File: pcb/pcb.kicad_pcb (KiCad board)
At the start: 2 copper layers, 350 x 170 mm, 80 parts, among them J1 Conn_01x24, SW1 0, SW10 9, SW11 HYPHEN, SW12 CARET, SW13 YEN, SW14 AT, SW15 LBRACKET, SW16 SEMICOLON, SW17 COLON, SW18 RBRACKET, SW19 COMMA, SW2 1, SW20 FULLSTOP, SW21 SLASH, SW22 UNDERSCORE, SW23 A, SW24 B, SW25 C, SW26 D, SW27 E, SW28 F, SW29 G, SW3 2, SW30 H, SW31 I, SW32 J, SW33 K, SW34 L, SW35 M, SW36 N, SW37 O, SW38 P, SW39 Q, SW4 3, SW40 R, SW41 PAUSE, SW42 S, SW43 T, SW44 U, SW45 V, SW46 W, SW47 X, SW48 Y, SW49 Z, SW5 4, SW50 LSHIFT, SW51 CTRL, SW52 GRAPH, SW53 CAP, SW54 KANA, SW55 F1/F6, SW56 F2/F7, SW57 F3/F8, SW58 RSHIFT, SW59 F4/F9, SW6 5, SW60 F5/F10, SW61 ESC, SW62 TAB, SW63 STOP, SW64 BS, SW65 SELECT, SW66 RETURN, SW67 SPACE, SW68 HOME, SW69 INS, SW7 6, SW70 DEL, SW71 LEFT, SW72 UP, SW73 DOWN, SW74 RIGHT, SW8 7, SW9 8

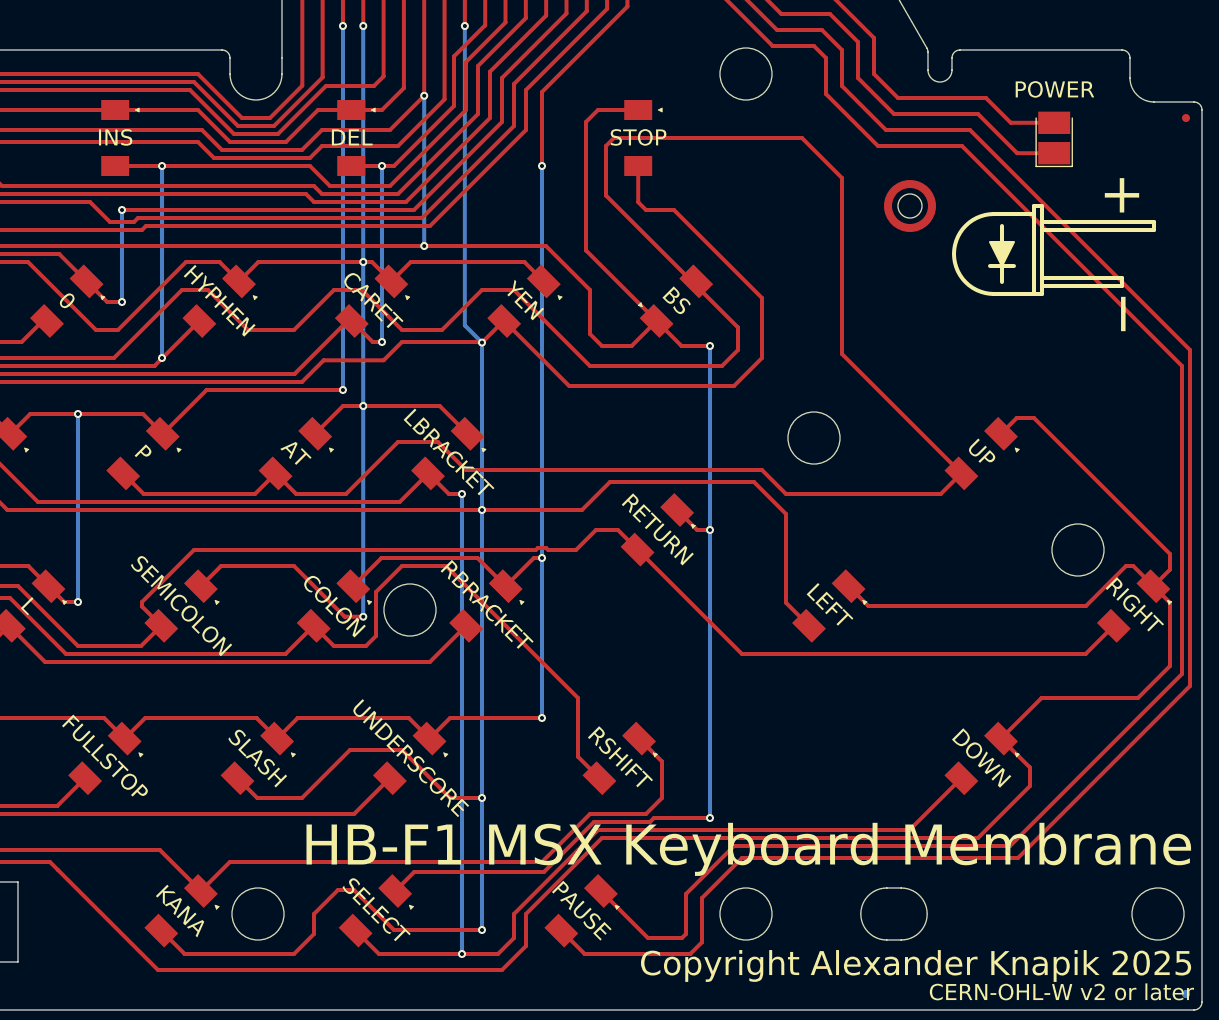
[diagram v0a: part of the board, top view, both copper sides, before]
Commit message: Updated PCB to Support HBF1II
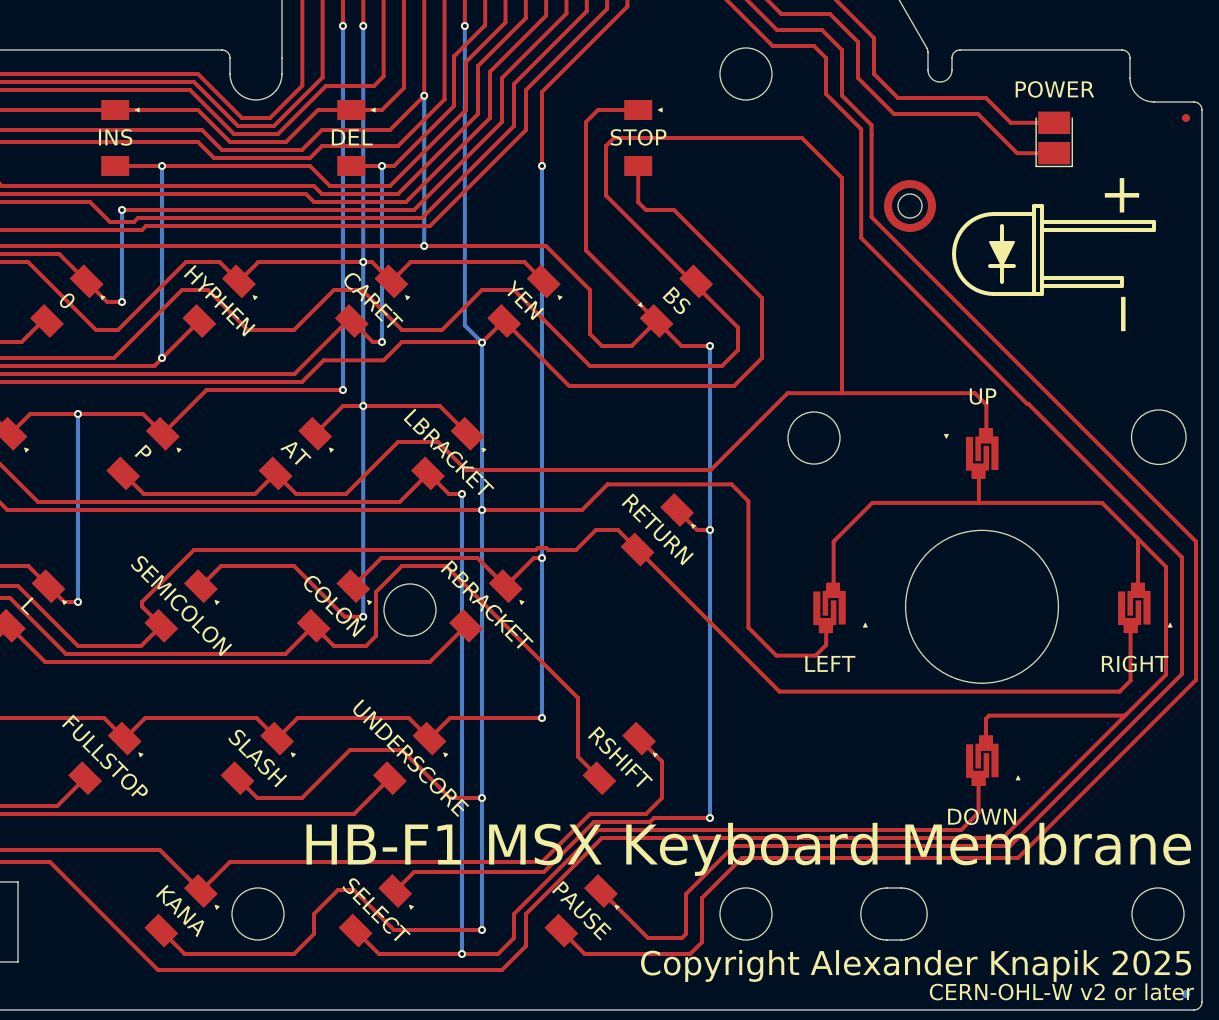
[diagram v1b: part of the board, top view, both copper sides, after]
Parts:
- SW71, SW72, SW73, SW74: footprint Sony_Hit_Bit:Switch -> Sony_Hit_Bit:Switch 2
- moved SW73 0.49 mm to (356.0, 207.0), turned to 180 degrees
- moved SW71 0.43 mm to (336.9, 187.9), turned to 180 degrees
- moved SW74 0.43 mm to (375.0, 187.9), turned to 180 degrees
- moved SW72 0.25 mm to (356.1, 168.3), turned to 0 degrees
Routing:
- net /2: track 705.2 -> 714.8 mm
- net /9: track 756.7 -> 765.8 mm
- net /5: track 1023.7 -> 1016.8 mm
- net Net-(J1-Pin_21): track 229.8 -> 223.8 mm
- net Net-(J1-Pin_22): track 236.2 -> 230.7 mm
- net /1: track 698.3 -> 702.5 mm
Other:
- outline, holes or cut-outs redrawn

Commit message: Added Render and cleaned up traces
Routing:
- net /6: track 549.4 -> 550.3 mm
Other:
- board text added: "HB-F1II MSX Keyboard Membrane"
- board text removed: "HB-F1 MSX Keyboard Membrane"
